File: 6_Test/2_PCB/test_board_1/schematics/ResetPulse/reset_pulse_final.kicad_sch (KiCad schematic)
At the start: 2 parts, among them U1 CD4001BM96, U2 SN74HC74DR

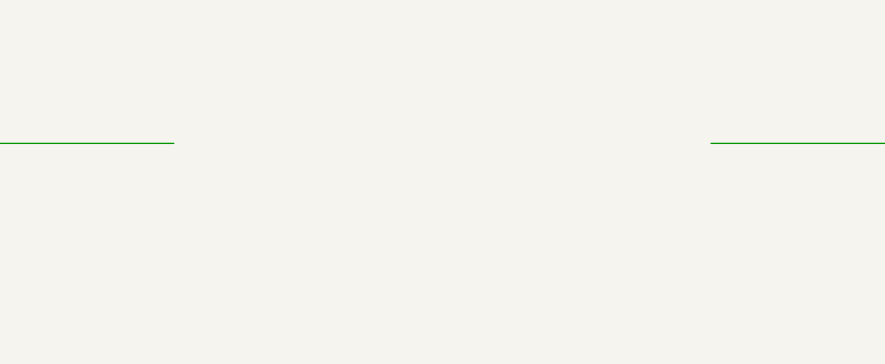
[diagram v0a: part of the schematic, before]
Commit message: fixed digital supply, added three sheets to board main
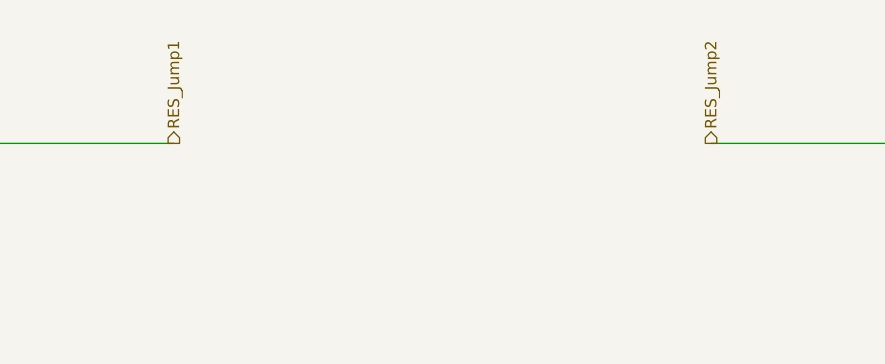
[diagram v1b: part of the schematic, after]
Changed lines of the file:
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@@
+		)
+	)
+	(hierarchical_label "RES_Jump1"
+		(shape output)
+		(at 177.8 44.45 90)
+		(fields_autoplaced yes)
+		(effects
+			(font
+				(size 1.27 1.27)
+			)
+			(justify left)
 		)
 	)
@@
 		)
 	)
+	(hierarchical_label "RES_Jump2"
+		(shape output)
+		(at 237.49 44.45 90)
+		(fields_autoplaced yes)
+		(effects
+			(font
+				(size 1.27 1.27)
+			)
+			(justify left)
+		)
+	)

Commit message: final draft of board done.
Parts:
- added J?: TSM-102-01-L-DV-P-TR, CONN_TSM-102-01-L-DV-P-TR_SAI, symbol 2x2Header:TSM-102-01-L-DV-P-TR
- renumbered U1 to U?, U2 to U?
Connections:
- net GND: now also U?.7 (GND)
- net RES: now also J?.2, J?.4; no longer U?.11 (M)
- net RESX: now also J?.3
- net VCC renamed V_SUP
- new net: J?.1, U?.11 (M)
